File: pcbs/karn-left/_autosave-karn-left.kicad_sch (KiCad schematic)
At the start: 45 parts, among them J1 S2B-PH-K-SLFSN, SW11 SW_Push, SW12 SW_Push, SW13 SW_Push, SW14 SW_Push, SW15 SW_Push, SW21 SW_Push, SW22 SW_Push, SW23 SW_Push, SW24 SW_Push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

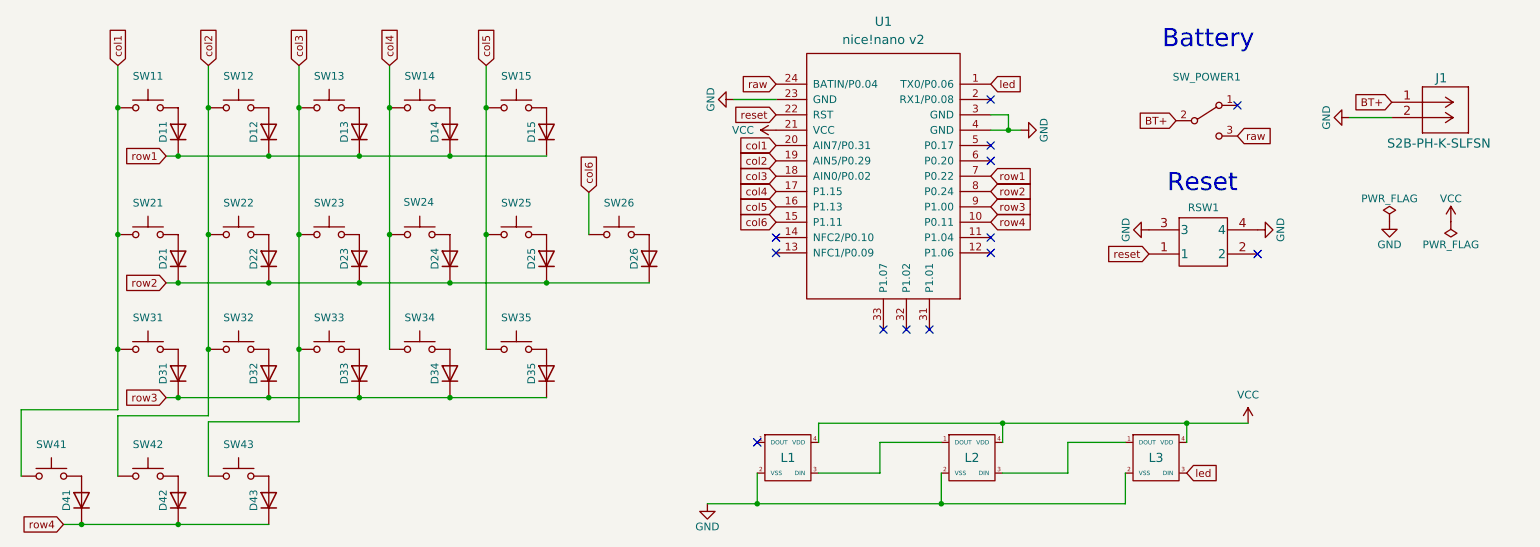
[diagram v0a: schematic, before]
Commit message: Update karn-left pcb
- Apply various fixes from lessons learned on karn-right
- Fix incorrectly oriented reset switch
- Swap incorrect default polarity of JST connector footprint
- Increase size of diode pads
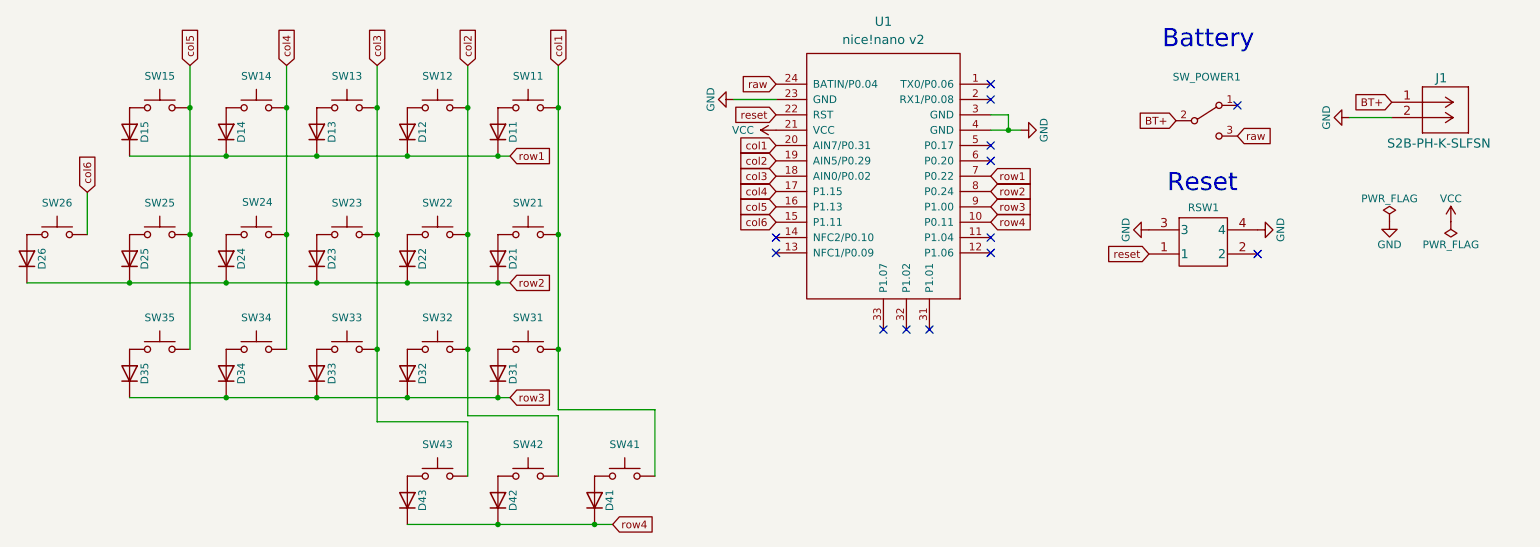
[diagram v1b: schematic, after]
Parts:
- removed L1, L2, L3: SK6812MINI, LED_SMD:LED_SK6812MINI_PLCC4_3.5x3.5mm_P1.75mm, symbol kbd:SK6812MINI
- J1: footprint kbd:S2B-PH-K-SLFSN -> karn-kicad:battery-connector-S2B-PH-K-SLFSN; symbol S2B-PH-K-SLFSN:S2B-PH-K-SLFSN -> karn-symbols:battery-connector-S2B-PH-K-SLFSN
- U1: symbol nice_nano:nice_nano -> karn-symbols:nice_nano
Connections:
- net led: no longer names the net of U1.1 (TX0/P0.06)
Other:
- moved on the sheet: D11, D12, D13, D14, D15, D21, D22, D23, D24, D25, D26, D31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
